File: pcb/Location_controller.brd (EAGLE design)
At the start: 100 x 80 mm, 8 parts, among them IC1 LIS302DL, U1 L3G4200DH

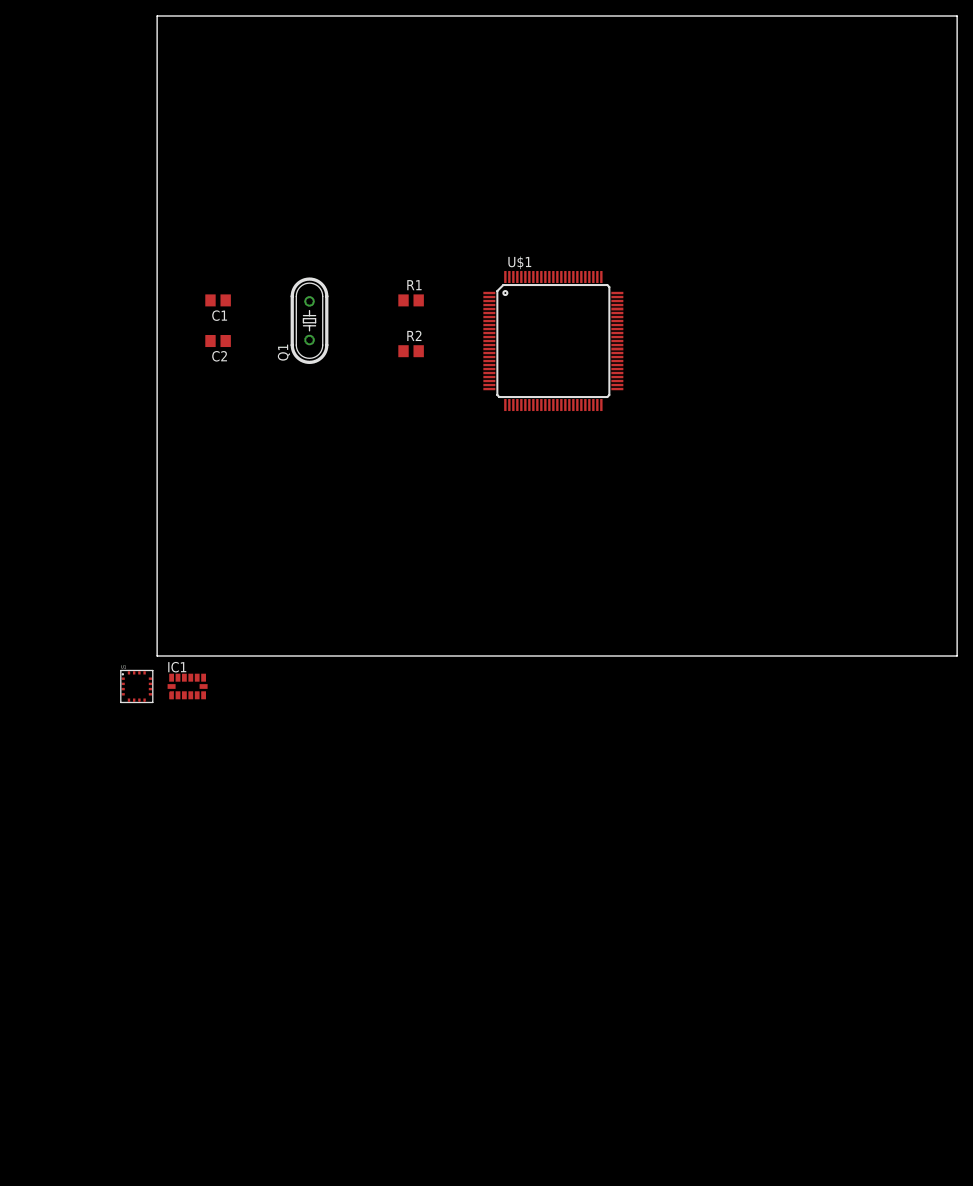
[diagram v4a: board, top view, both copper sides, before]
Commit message: Add Voltage Regulator and application circuits
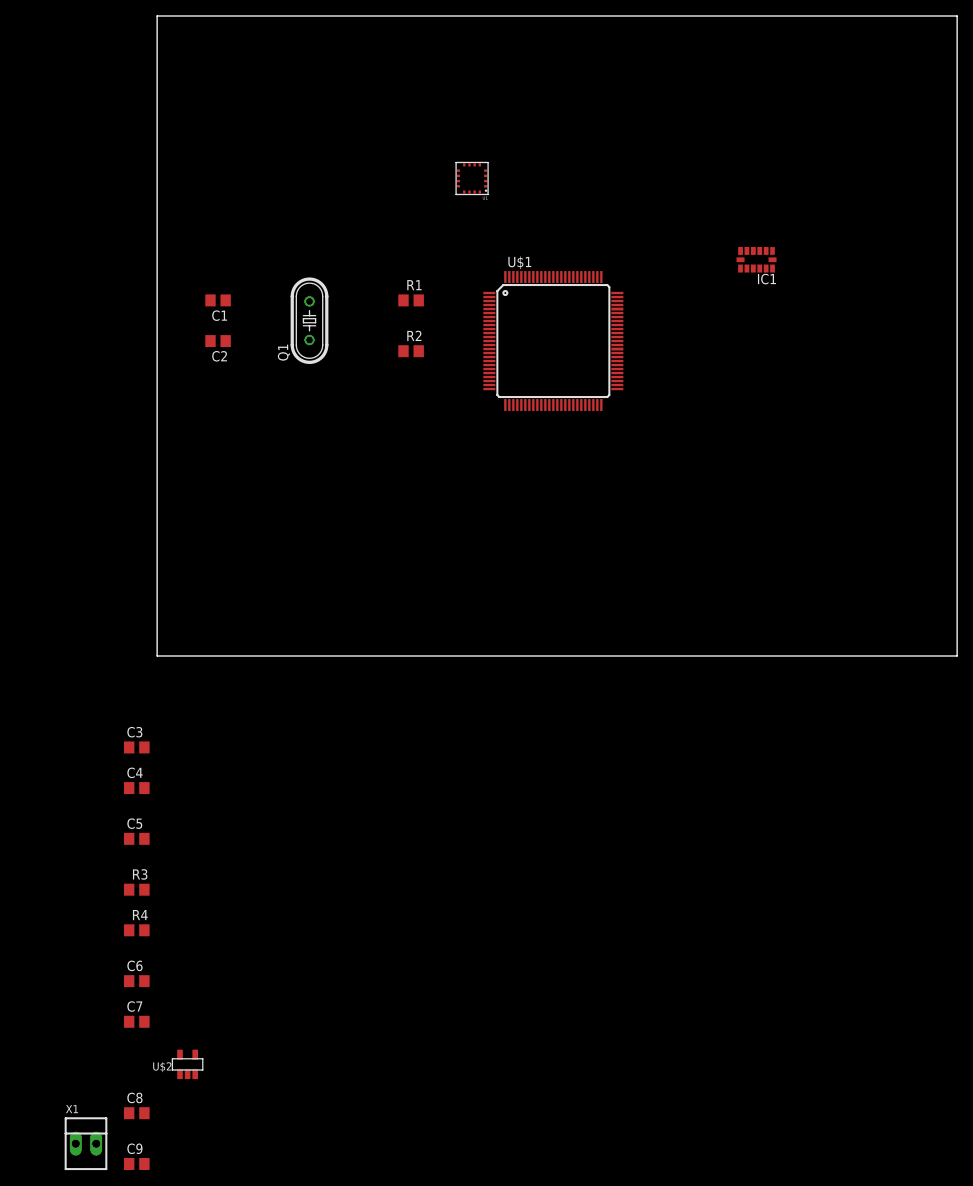
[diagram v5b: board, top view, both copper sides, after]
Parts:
- added C3, C6: 10u, eagle-ltspice:C0805
- added C4, C7, C8, C9: 100n, eagle-ltspice:C0805
- added C5: 10n (25V ceramic), eagle-ltspice:C0805
- added R3, R4: 10k, eagle-ltspice:R0805
- added U$2: NCP551, stm32f4:TSOP-5
- added X1: 22-23-2021, con-molex:22-23-2021
- moved IC1 88.9 mm to (74.9, 49.5), turned to 180 degrees
- moved U1 76.1 mm to (39.4, 59.7), turned to 180 degrees
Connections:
- removed net RES(GND): U1.10, U1.11, U1.12, U1.8, U1.9
- removed net RES(VDD): U1.15
- removed net VDD_IO: IC1.1, U1.1
- new net I2C_SCL: IC1.14, R3.2, U$1.92, U1.2
- new net I2C_SDA: IC1.13, R4.2, U$1.93, U1.3
- new net N$3: C5.1, U1.14
- new net N$4: C8.1, U$2.1, U$2.3, X1.1
- net GND: now also C3.2, C4.2, C5.2, C6.2, C7.2, C8.2, C9.2, IC1.10, IC1.11, IC1.4, IC1.5, U$2.2, U1.10, U1.11, U1.12, U1.4, U1.8, U1.9, X1.2
- net VDD: now also C3.1, C4.1, C6.1, C7.1, C9.1, IC1.1, IC1.12, IC1.3, IC1.7, R3.1, R4.1, U$2.5, U1.1, U1.15, U1.5

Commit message: Add decoupling to schematic + initial layout
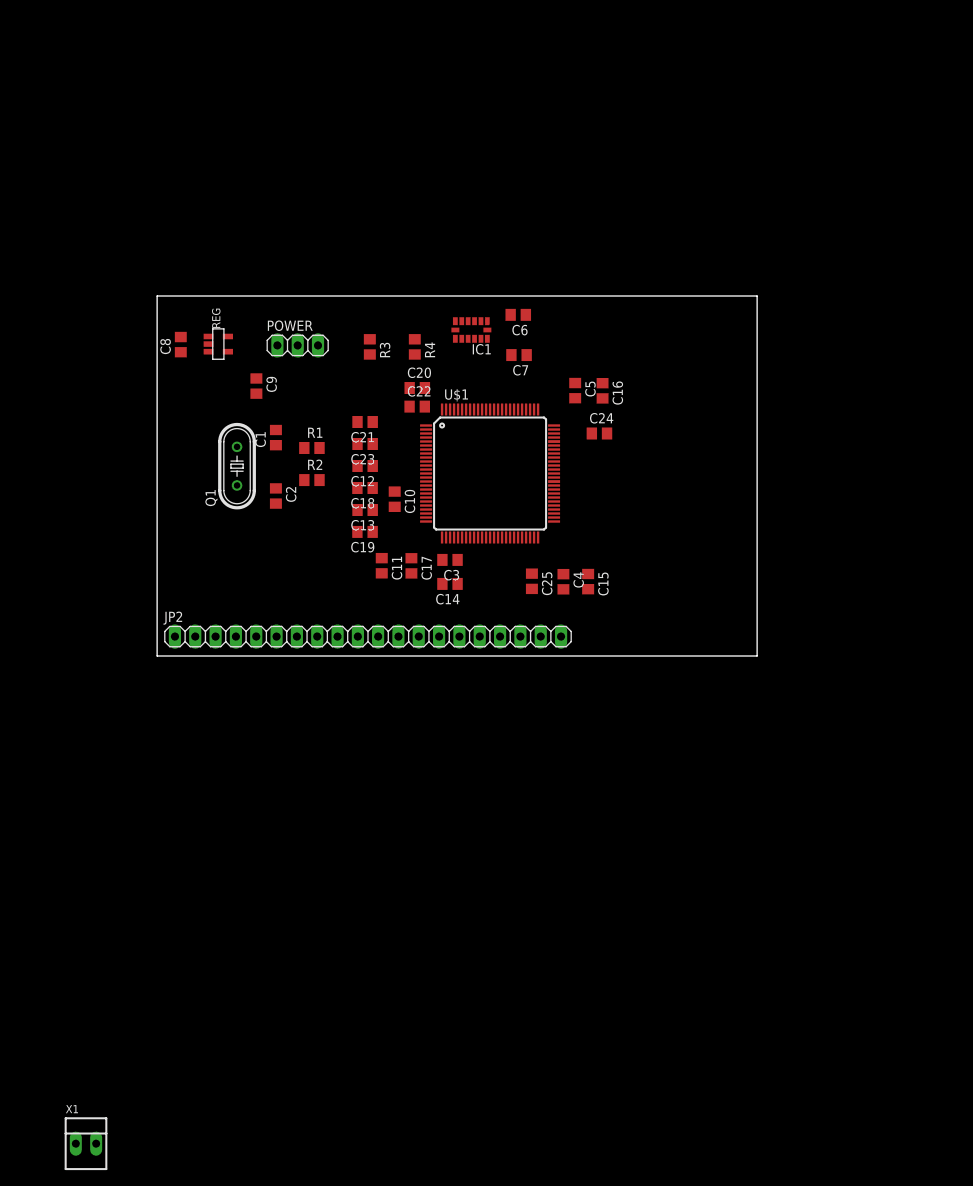
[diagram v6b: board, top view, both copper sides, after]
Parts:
- removed U$2: NCP551, stm32f4:TSOP-5
- removed U1: L3G4200DH, stm32f4:LGA-16L
- added C10: 100n, eagle-ltspice:C0805
- added C11, C12, C13, C20, C21: 1u, eagle-ltspice:C0805
- added C14, C15, C16, C17, C18, C19, C22, C23: 10n, eagle-ltspice:C0805
- added C24, C25: 2.2u, eagle-ltspice:C0805
- added JP2: (no value), pinhead:1X20
- added POWER: (no value), pinhead:1X03
- added REG: NCP551, stm32f4:TSOP-5
- C3: value 10u -> 1u
- C4: value 100n -> 1u
- C5: value 10n (25V ceramic) -> 1u
- moved C9 98.4 mm to (12.4, 33.7), turned to 270 degrees
- moved C8 96.2 mm to (2.96, 38.9), turned to 90 degrees
- moved C7 96.1 mm to (45.2, 37.6), turned to 180 degrees
- moved C6 96.0 mm to (45.1, 42.6), turned to 180 degrees
- moved R4 80.8 mm to (32.2, 38.6), turned to 270 degrees
- moved C5 78.4 mm to (52.3, 33.2), turned to 270 degrees
- moved R3 73.8 mm to (26.6, 38.6), turned to 270 degrees
- moved C4 59.2 mm to (50.8, 9.28), turned to 270 degrees
- moved C3 45.6 mm to (36.6, 12.0), turned to 180 degrees
- moved IC1 36.7 mm to (39.3, 40.8)
- moved R1 22.2 mm to (19.4, 26.0)
- moved C2 20.7 mm to (14.8, 20.0), turned to 270 degrees
- moved R2 20.3 mm to (19.4, 22.0)
- moved Q1 20.3 mm to (9.99, 23.7)
- moved C1 18.6 mm to (14.8, 27.3), turned to 90 degrees
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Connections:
- removed net N$3: C5.1, U1.14
- new net N$10: C9.1, POWER.1, REG.5
- new net N$5: C10.1, U$1.14
- new net N$8: C25.1, U$1.49
- new net N$9: C24.1, U$1.73
- net GND: now also C10.2, C11.2, C12.2, C13.2, C14.2, C15.2, C16.2, C17.2, C18.2, C19.2, C20.2, C21.2, C22.2, C23.2, C24.2, C25.2, REG.2, U$1.10, U$1.20, U$1.27, U$1.74, U$1.99; no longer U$2.2, U1.10, U1.11, U1.12, U1.13, U1.4, U1.8, U1.9
- net I2C_SCL: now also R4.2; no longer R3.2, U1.2
- net I2C_SDA: now also R3.2; no longer R4.2, U1.3
- net N$4: now also REG.1, REG.3; no longer U$2.1, U$2.3
- net VDD: now also C11.1, C12.1, C13.1, C14.1, C15.1, C16.1, C17.1, C18.1, C19.1, C20.1, C21.1, C22.1, C23.1, C5.1, POWER.2, U$1.100, U$1.11, U$1.19, U$1.21, U$1.22, U$1.28, U$1.50, U$1.75; no longer C9.1, U$2.5, U1.1, U1.15, U1.16, U1.5
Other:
- board size 100 x 80 mm -> 75 x 45 mm
- board text added: "BAT"
- board text added: "DRN"

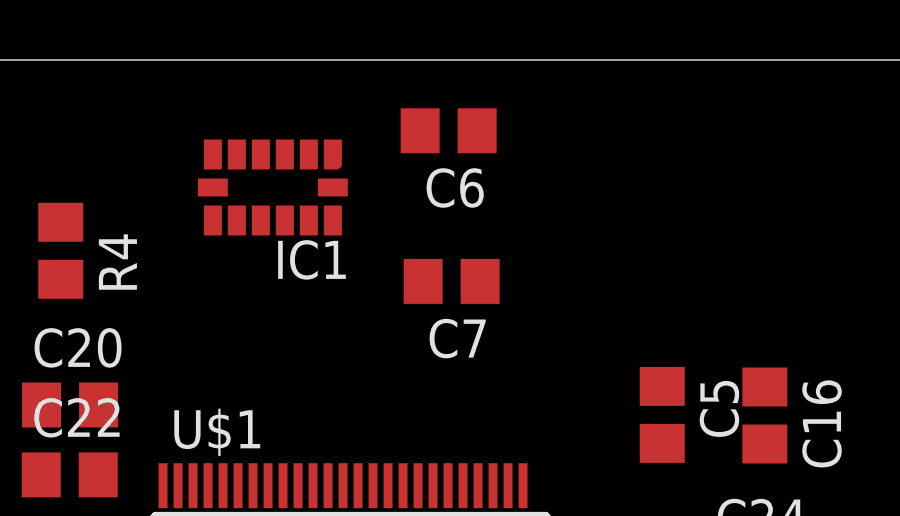
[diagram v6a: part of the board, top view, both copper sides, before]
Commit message: Add connections to RCM
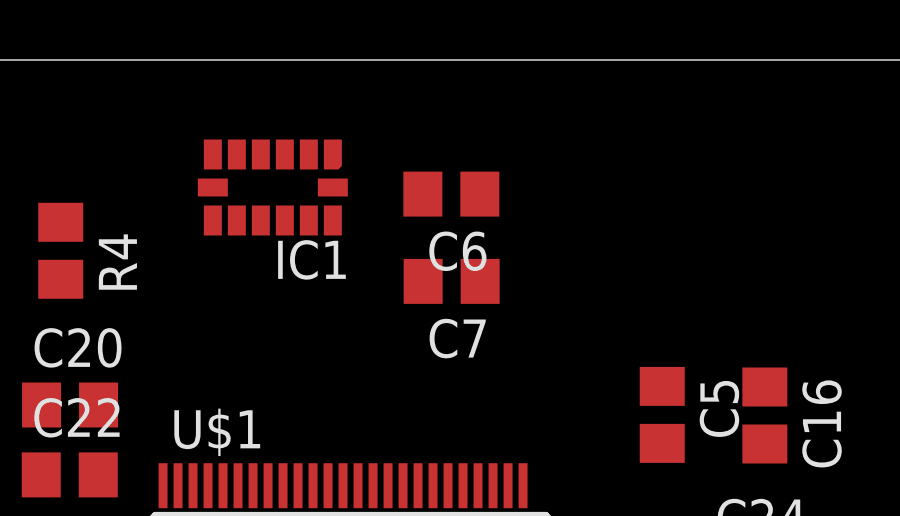
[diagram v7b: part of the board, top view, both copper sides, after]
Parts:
- moved C6 2.11 mm to (45.2, 40.5)
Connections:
- new net USART2_RX: JP2.19, U$1.26
- new net USART2_TX: JP2.18, U$1.25
- net GND: now also JP2.15

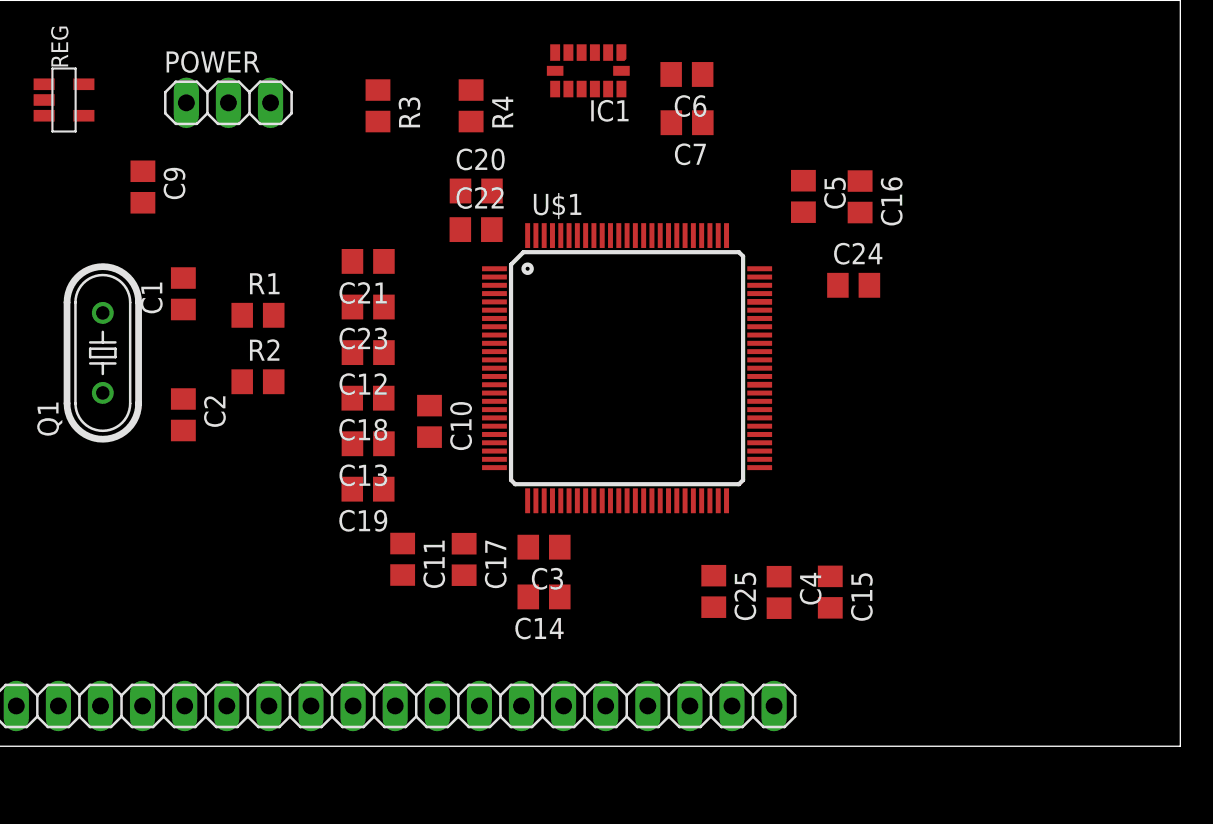
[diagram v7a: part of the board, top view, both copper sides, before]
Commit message: Add SWD programmer connectors
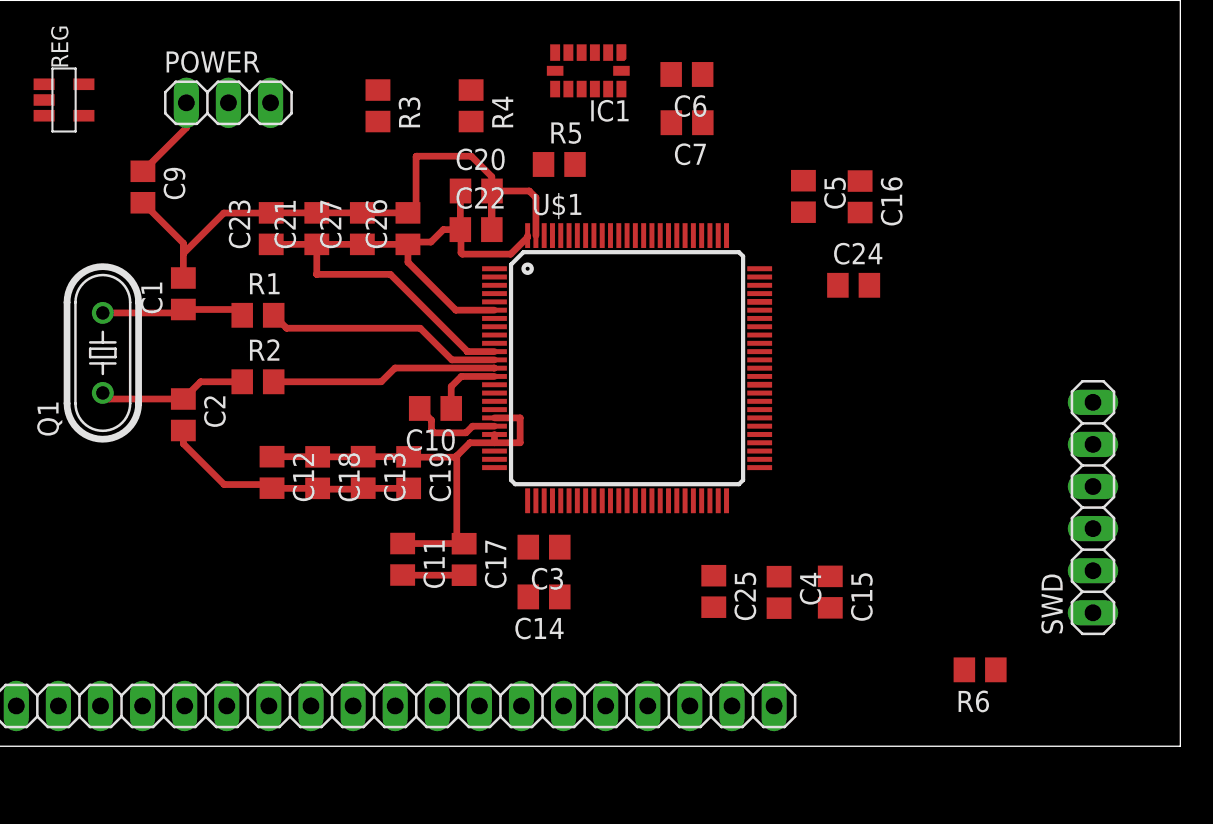
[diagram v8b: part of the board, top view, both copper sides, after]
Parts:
- added C26: 10n, eagle-ltspice:C0805
- added C27: 1u, eagle-ltspice:C0805
- added R5: 10k, eagle-ltspice:R0805
- added R6: 0, eagle-ltspice:R0805
- added SWD: (no value), pinhead:1X06
- moved C12 9.27 mm to (20.2, 16.5), turned to 270 degrees
- moved C23 7.52 mm to (20.1, 31.2), turned to 90 degrees
- moved C18 5.42 mm to (22.9, 16.5), turned to 270 degrees
- moved C21 3.68 mm to (22.9, 31.2), turned to 90 degrees
- moved C19 2.65 mm to (28.4, 16.5), turned to 270 degrees
- moved C13 1.76 mm to (25.7, 16.5), turned to 270 degrees
- moved C10 0.86 mm to (30.1, 20.4), turned to 180 degrees
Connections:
- removed net N$5: C10.1, U$1.14
- new net N$3: R5.2, U$1.94
- new net N$6: R6.1, SWD.1
- new net NRST: C10.1, SWD.5, U$1.14
- new net SWCLK: SWD.2, U$1.76
- new net SWDIO: SWD.4, U$1.72
- new net SWO: SWD.6, U$1.89
- net GND: now also C26.2, C27.2, SWD.3
- net VDD: now also C26.1, C27.1, R5.1, R6.2, U$1.6
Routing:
- net VDD: track 0.00 -> 70.5 mm
- net GND: track 0.00 -> 64.4 mm
- net OSC_IN: track 0.00 -> 14.4 mm
- net OSC_OUT: track 0.00 -> 13.7 mm
- net N$1: track 0.00 -> 8.99 mm
- net N$2: track 0.00 -> 8.64 mm
- net N$10: track 0.00 -> 5.22 mm
- net NRST: track 0.00 -> 4.18 mm
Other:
- board text added: "GND"
- board text added: "NRST"
- board text added: "SWCLK"
- board text added: "SWDIO"
- board text added: "SWO"
- board text added: "VDD"
